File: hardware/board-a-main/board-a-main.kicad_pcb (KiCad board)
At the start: 2 copper layers, 50 x 35 mm, 23 parts, among them J1 USB_C_Receptacle_USB2.0_16P, J2 Conn_01x08, J3 Conn_01x04, U1 STM32F446RETx, U2 USBLC6-2SC6, U3 AP2112K-3.3

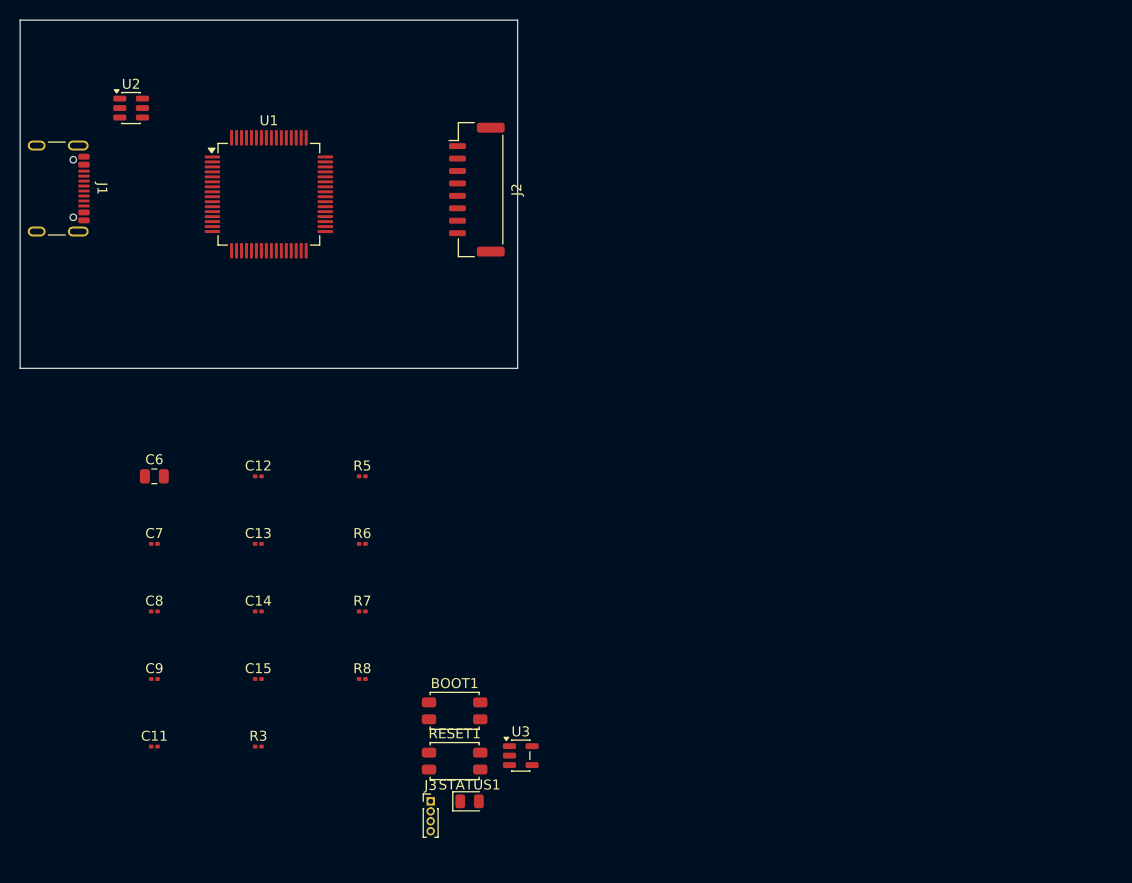
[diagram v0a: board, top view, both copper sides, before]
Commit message: Complete Board A PCB layout
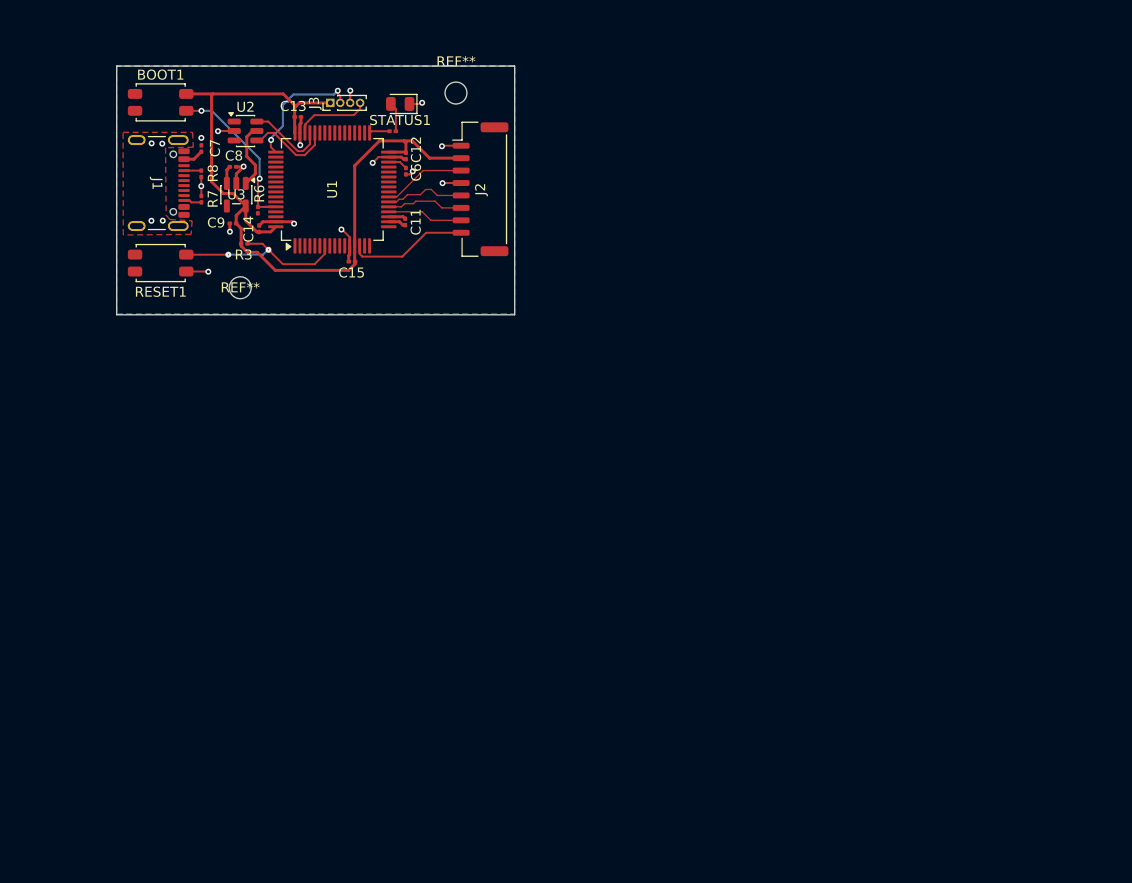
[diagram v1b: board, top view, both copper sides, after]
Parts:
- added REF**: MountingHole_2.2mm_M2, MountingHole:MountingHole_2.2mm_M2, F.Cu at (99.0, 36.5)
- added REF**: MountingHole_2.2mm_M2, MountingHole:MountingHole_2.2mm_M2, F.Cu at (77.3, 56.0)
- C15: value 100nf -> 10uf
- C6: footprint Capacitor_SMD:C_0805_2012Metric -> Capacitor_SMD:C_0201_0603Metric
- moved J3 70.9 mm to (86.4, 37.5), turned to 90 degrees
- moved STATUS1 70.4 mm to (93.4, 37.6), turned to 180 degrees
- moved BOOT1 67.9 mm to (69.3, 37.4)
- moved U3 63.2 mm to (76.9, 46.7), turned to -90 degrees
- moved C11 58.4 mm to (93.9, 49.4), turned to 90 degrees
- moved RESET1 58.1 mm to (69.3, 53.6)
- moved R8 53.3 mm to (73.4, 44.6), turned to -90 degrees
- moved R3 50.6 mm to (77.8, 51.6)
- moved C9 46.5 mm to (76.6, 49.6), turned to 180 degrees
- moved C8 45.4 mm to (76.6, 43.9), turned to 180 degrees
- moved R7 44.5 mm to (73.4, 47.1), turned to 90 degrees
- moved C13 43.1 mm to (83.1, 38.9), turned to 180 degrees
- moved C15 43.0 mm to (88.6, 53.4)
- moved C7 40.0 mm to (73.4, 42.1), turned to -90 degrees
- moved C6 39.7 mm to (94.0, 44.3), turned to -90 degrees
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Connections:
- J2 pad 3: /IMU_SPI_SCK -> /IMU_SPI_MOSI
- J2 pad 6: /IMU_SPI_MOSI -> /IMU_SPI_SCK
- R5 pad 2: Net-(U1-PB8) -> Net-(U1-PB12)
- U1 pad 33: unconnected-(U1-PB12-Pad33) -> Net-(U1-PB12)
- U1 pad 61: Net-(U1-PB8) -> unconnected-(U1-PB8-Pad61)
- U2 pad 1: Net-(J1-D--PadA7) -> Net-(J1-D+-PadA6)
- U2 pad 3: Net-(J1-D+-PadA6) -> Net-(J1-D--PadA7)
- U2 pad 4: /USB_DP -> /USB_DM
- U2 pad 6: /USB_DM -> /USB_DP
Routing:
- net /3.3V: track 0.00 -> 80.9 mm
- net GND: track 0.00 -> 32.3 mm, vias 0 -> 19
- net Net-(U1-NRST): track 0.00 -> 18.6 mm, vias 0 -> 2
- net Net-(U1-BOOT0): track 0.00 -> 17.2 mm, vias 0 -> 2
- net /SWCLK: track 0.00 -> 12.9 mm, vias 0 -> 2
- net /IMU_INT: track 0.00 -> 12.1 mm
- net /5VBUS: track 0.00 -> 10.5 mm
- net /USB_DM: track 0.00 -> 8.69 mm
- net /IMU_SPI_MOSI: track 0.00 -> 8.37 mm
- net /IMU_SPI_MISO: track 0.00 -> 8.04 mm
- net /USB_DP: track 0.00 -> 7.98 mm
- net /IMU_SPI_SCK: track 0.00 -> 7.79 mm
- net /SWDIO: track 0.00 -> 7.65 mm
- net /IMU_CS: track 0.00 -> 7.63 mm
- net Net-(STATUS1-A): track 0.00 -> 2.95 mm
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- added copper zone on B.Cu, net GND
- added copper zone on F.Cu, net GND
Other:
- board size 50 x 35 mm -> 40 x 25 mm

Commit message: Board B schematic and PCB layout
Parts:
- moved C2 81.5 mm to (136.7, 99.0)
- moved C4 81.5 mm to (148.6, 108.5)
- moved C5 81.5 mm to (139.3, 105.2)
- moved C6 81.5 mm to (143.2, 94.0)
- moved J2 81.5 mm to (161.5, 101.2)
- moved R1 81.5 mm to (133.5, 99.7)
- moved R3 81.5 mm to (137.8, 106.7)
- moved R5 81.5 mm to (152.7, 95.4)
- moved REF** 81.5 mm to (159.1, 91.6)
- moved STATUS1 81.5 mm to (153.5, 92.7)
- moved C3 81.5 mm to (136.7, 104.7)
- moved C7 81.5 mm to (154.0, 97.9)
- moved C8 81.5 mm to (154.0, 104.5)
- moved C9 81.5 mm to (154.0, 99.4)
- moved J1 81.5 mm to (128.1, 100.6)
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- renumbered C7 to C1, C8 to C2, C9 to C3, C15 to C4, C14 to C5, C13 to C6, C12 to C7, C11 to C8, C6 to C9, R8 to R1, R7 to R2, R6 to R4, U2 to U1, U3 to U2, U1 to U3
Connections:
- C9 pad 1: Net-(U1-VCAP_1) -> (no net)
- U2 pad 4: unconnected-(U3-NC-Pad4) -> (no net)
- U3 pad 10: unconnected-(U1-PC2-Pad10) -> (no net)
- U3 pad 11: unconnected-(U1-PC3-Pad11) -> (no net)
- U3 pad 15: unconnected-(U1-PA1-Pad15) -> (no net)
- U3 pad 16: unconnected-(U1-PA2-Pad16) -> (no net)
- U3 pad 17: unconnected-(U1-PA3-Pad17) -> (no net)
- U3 pad 2: unconnected-(U1-PC13-Pad2) -> (no net)
- U3 pad 24: unconnected-(U1-PC4-Pad24) -> (no net)
- U3 pad 25: unconnected-(U1-PC5-Pad25) -> (no net)
- U3 pad 26: unconnected-(U1-PB0-Pad26) -> (no net)
- U3 pad 27: unconnected-(U1-PB1-Pad27) -> (no net)
- U3 pad 28: unconnected-(U1-PB2-Pad28) -> (no net)
- U3 pad 29: unconnected-(U1-PB10-Pad29) -> (no net)
- U3 pad 3: unconnected-(U1-PC14-Pad3) -> (no net)
- U3 pad 30: Net-(U1-VCAP_1) -> Net-(U3-VCAP_1)
- U3 pad 34: unconnected-(U1-PB13-Pad34) -> (no net)
- U3 pad 35: unconnected-(U1-PB14-Pad35) -> (no net)
- U3 pad 36: unconnected-(U1-PB15-Pad36) -> (no net)
- U3 pad 37: unconnected-(U1-PC6-Pad37) -> (no net)
- U3 pad 38: unconnected-(U1-PC7-Pad38) -> (no net)
- U3 pad 39: unconnected-(U1-PC8-Pad39) -> (no net)
- U3 pad 4: unconnected-(U1-PC15-Pad4) -> (no net)
- U3 pad 40: unconnected-(U1-PC9-Pad40) -> (no net)
- U3 pad 41: unconnected-(U1-PA8-Pad41) -> (no net)
- U3 pad 42: unconnected-(U1-PA9-Pad42) -> (no net)
- U3 pad 43: unconnected-(U1-PA10-Pad43) -> (no net)
- U3 pad 5: unconnected-(U1-PH0-Pad5) -> (no net)
- U3 pad 50: unconnected-(U1-PA15-Pad50) -> (no net)
- U3 pad 51: unconnected-(U1-PC10-Pad51) -> (no net)
- U3 pad 52: unconnected-(U1-PC11-Pad52) -> (no net)
- U3 pad 53: unconnected-(U1-PC12-Pad53) -> (no net)
- U3 pad 54: unconnected-(U1-PD2-Pad54) -> (no net)
- U3 pad 55: unconnected-(U1-PB3-Pad55) -> (no net)
- U3 pad 56: unconnected-(U1-PB4-Pad56) -> (no net)
- U3 pad 57: unconnected-(U1-PB5-Pad57) -> (no net)
- U3 pad 58: unconnected-(U1-PB6-Pad58) -> (no net)
- U3 pad 59: unconnected-(U1-PB7-Pad59) -> (no net)
- U3 pad 6: unconnected-(U1-PH1-Pad6) -> (no net)
- U3 pad 61: unconnected-(U1-PB8-Pad61) -> (no net)
- U3 pad 62: unconnected-(U1-PB9-Pad62) -> (no net)
- U3 pad 8: unconnected-(U1-PC0-Pad8) -> (no net)
- U3 pad 9: unconnected-(U1-PC1-Pad9) -> (no net)
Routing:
- net /3.3V: track 80.9 -> 89.5 mm
- net Net-(J1-D--PadA7): track 0.00 -> 2.76 mm
- net Net-(J1-D+-PadA6): track 0.00 -> 2.72 mm
- net Net-(U3-VCAP_1): track 0.00 -> 1.97 mm
- net Net-(U1-VCAP_1): track 1.97 -> 0.00 mm

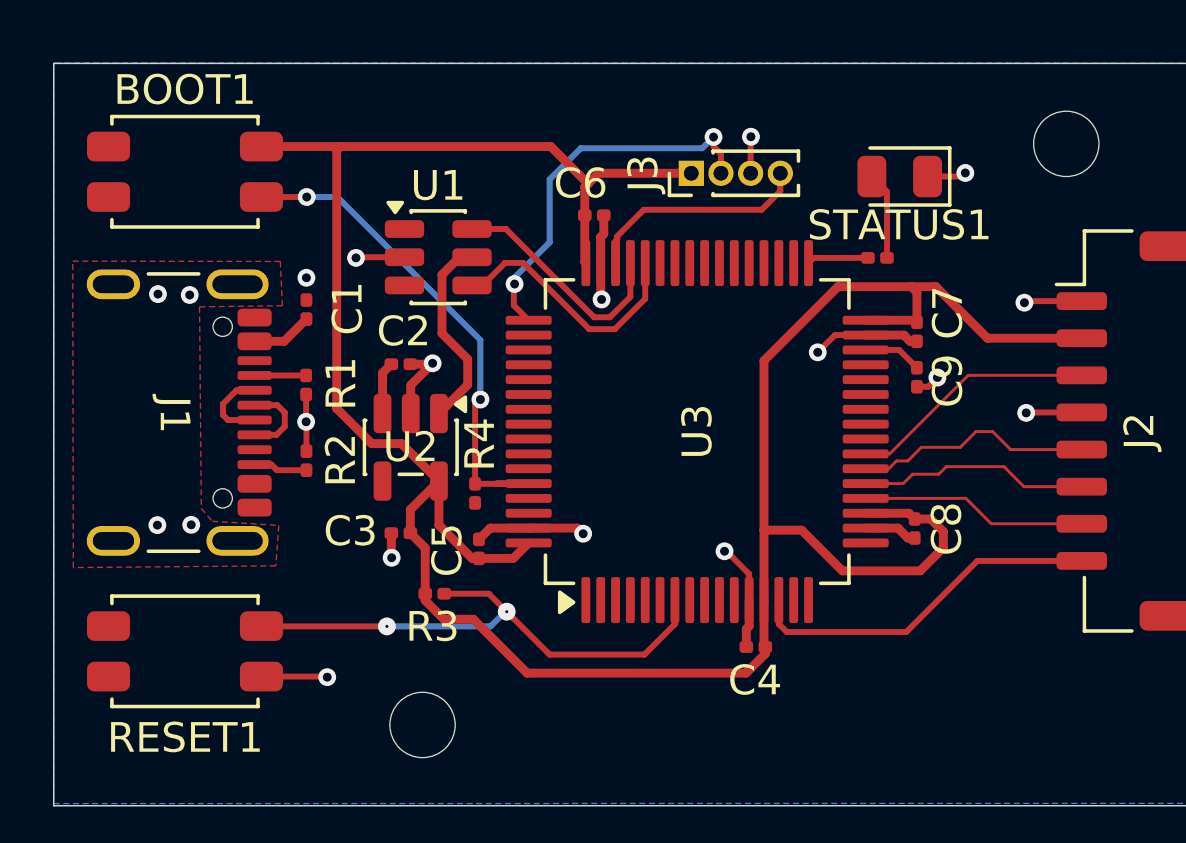
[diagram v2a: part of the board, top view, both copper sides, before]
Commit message: Add exported schematics, PCB layouts, and BOM
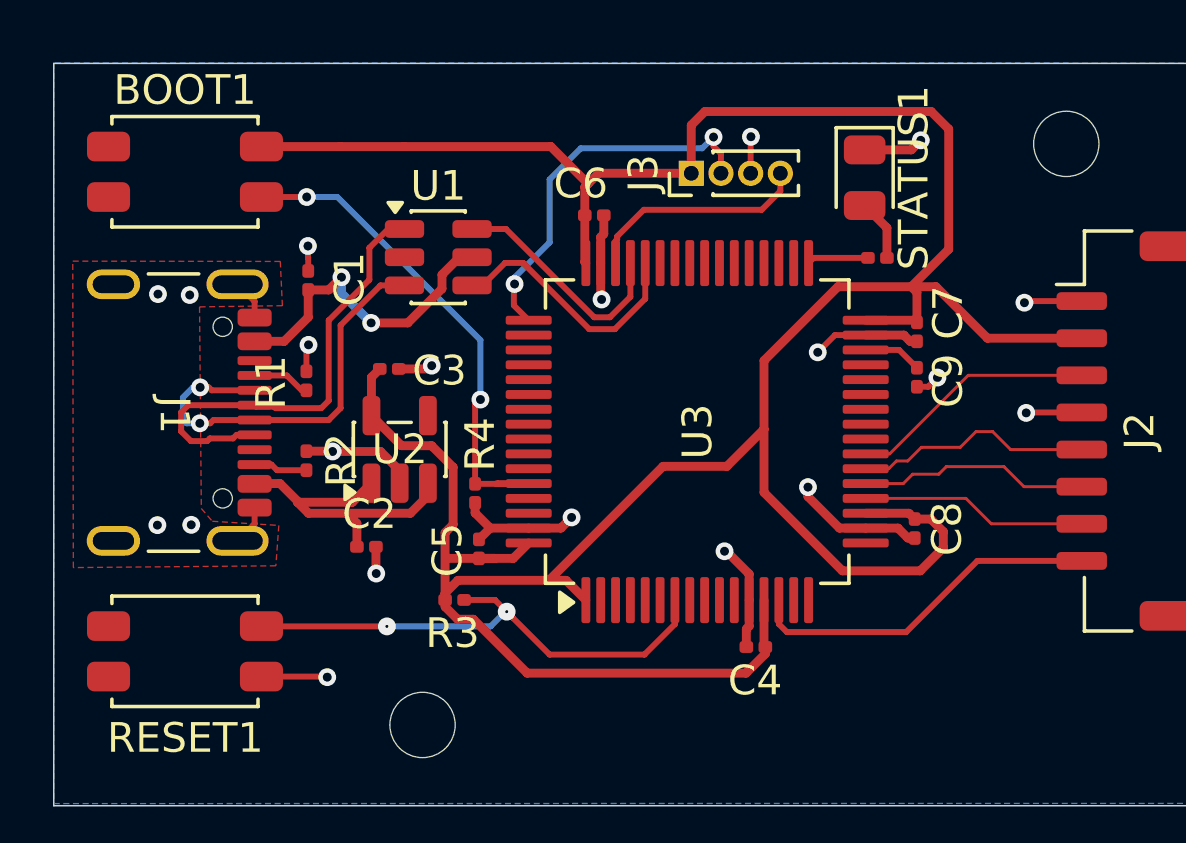
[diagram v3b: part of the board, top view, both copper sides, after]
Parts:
- moved C2 6.26 mm to (135.5, 105.2)
- moved C3 5.54 mm to (136.3, 99.2), turned to 0 degrees
- moved STATUS1 1.18 mm to (152.3, 92.7), turned to -90 degrees
- moved C1 0.98 mm to (133.5, 96.2)
- moved R3 0.70 mm to (138.5, 106.9)
- moved U2 0.38 mm to (136.6, 101.9), turned to 90 degrees
- moved R1 0.14 mm to (133.5, 99.6), turned to 90 degrees
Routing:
- net /3.3V: track 89.5 -> 107.3 mm
- net Net-(J1-D+-PadA6): track 2.72 -> 15.7 mm
- net Net-(J1-D--PadA7): track 2.76 -> 14.6 mm, vias 0 -> 2
- net /5VBUS: track 10.5 -> 21.9 mm, vias 0 -> 2
- net GND: track 32.3 -> 39.7 mm, vias 19 -> 20
- net Net-(U3-NRST): track 18.6 -> 17.6 mm
- net Net-(STATUS1-A): track 2.95 -> 2.07 mm
